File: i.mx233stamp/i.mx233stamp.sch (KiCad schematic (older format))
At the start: 0 parts

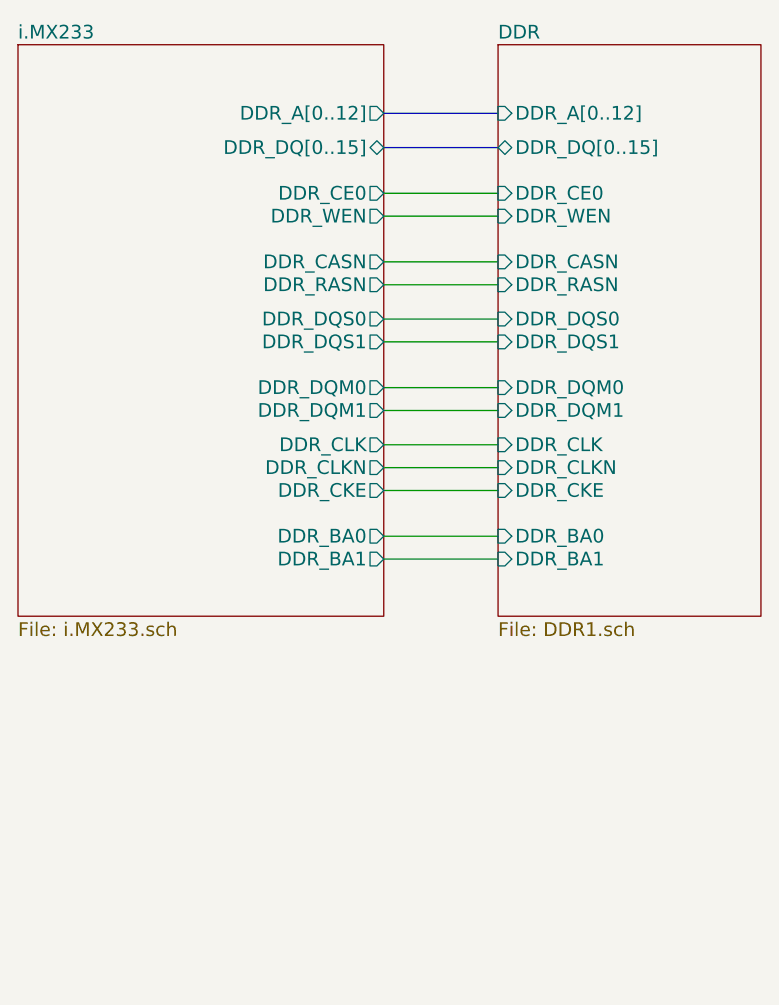
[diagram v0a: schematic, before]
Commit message: Added some connections to the pin header and the filters of the sources
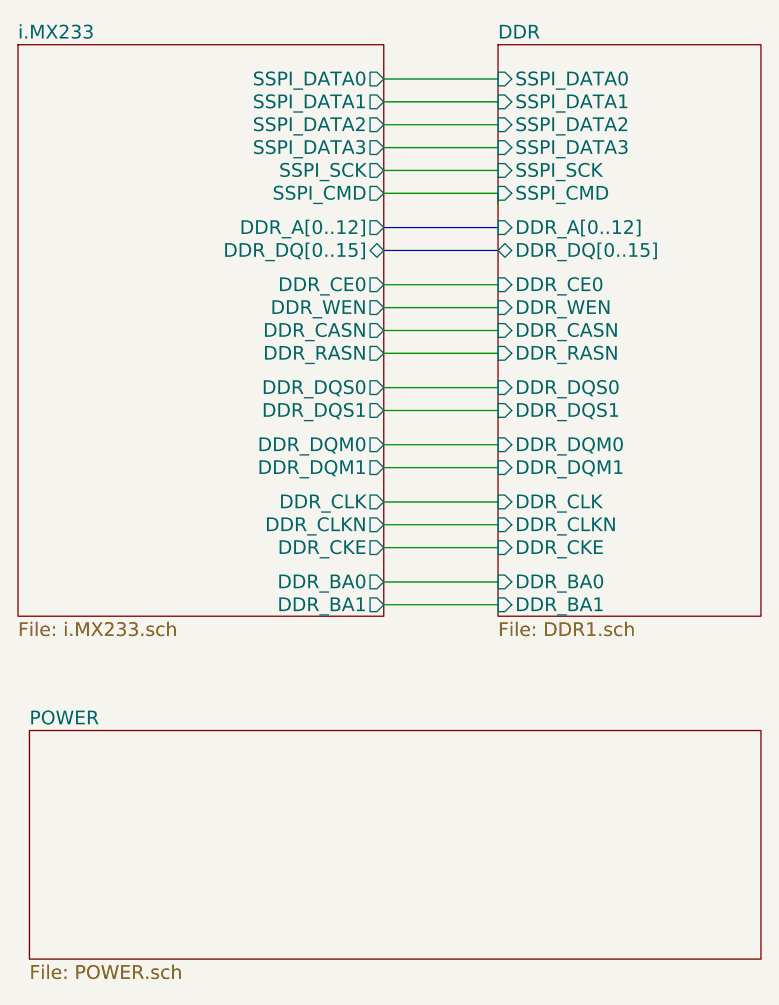
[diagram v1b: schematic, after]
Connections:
- wire segments 13 -> 20
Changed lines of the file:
@@
-EESchema Schematic File Version 2  date Thu 20 Jan 2011 08:06:53 AM COT
+EESchema Schematic File Version 2  date jue 27 ene 2011 16:12:42 COT
+LIBS:transistor-npn
+LIBS:ipc-7351-transistor
+LIBS:switch-misc
 LIBS:power
 LIBS:device
@@
 LIBS:EEPROM
 LIBS:PWR
+LIBS:m25p32
 LIBS:i.mx233stamp-cache
 EELAYER 24  0
 EELAYER END
 $Descr A4 11700 8267
-Sheet 1 3
+Sheet 1 4
 Title ""
-Date "20 jan 2011"
+Date "27 jan 2011"
 Rev ""
 Comp ""
@@
 Comment4 ""
 $EndDescr
+$Sheet
+S 3200 4600 3200 1000
+U 4D41BD76
+F0 "POWER" 60
+F1 "POWER.sch" 60
+$EndSheet
 Wire Wire Line
-	4750 3200 5250 3200
+	4750 2150 5250 2150
 Wire Wire Line
-	5250 2900 4750 2900
+	4750 1850 5250 1850
+Wire Bus Line
+	4750 2500 5250 2500
+Wire Wire Line
+	4750 2050 5250 2050
+Wire Wire Line
+	5250 3350 4750 3350
+Wire Wire Line
+	4750 3100 5250 3100
+Wire Wire Line
+	4750 3950 5250 3950
+Wire Wire Line
+	4750 3700 5250 3700
 Wire Wire Line
 	4750 2650 5250 2650
 Wire Wire Line
-	4750 3850 5250 3850
+	4750 2750 5250 2750
 Wire Wire Line
-	4750 3550 5250 3550
+	4750 2850 5250 2850
 Wire Wire Line
-	4750 3350 5250 3350
+	4750 3600 5250 3600
 Wire Wire Line
-	4750 2550 5250 2550
+	4750 3800 5250 3800
 Wire Wire Line
-	4750 2250 5250 2250
-Wire Bus Line
-	4750 1900 5250 1900
-Wire Bus Line
-	4750 2050 5250 2050
+	4750 4050 5250 4050
 Wire Wire Line
-	4750 2350 5250 2350
+	4750 2950 5250 2950
+Wire Wire Line
+	5250 3200 4750 3200
 Wire Wire Line
 	4750 3450 5250 3450
+Wire Bus Line
+	5250 2400 4750 2400
 Wire Wire Line
-	4750 3750 5250 3750
+	5250 1750 4750 1750
 Wire Wire Line
-	4750 2800 5250 2800
+	5250 1950 4750 1950
 Wire Wire Line
-	5250 3100 4750 3100
+	5250 2300 5250 2250
+Wire Wire Line
+	5250 2250 4750 2250
 $Sheet
 S 5250 1600 1150 2500
@@
 F0 "DDR" 60
 F1 "DDR1.sch" 60
-F2 "DDR_A[0..12]" I L 5250 1900 60
-F3 "DDR_DQ[0..15]" B L 5250 2050 60
-F4 "DDR_BA0" I L 5250 3750 60
-F5 "DDR_BA1" I L 5250 3850 60
-F6 "DDR_CE0" I L 5250 2250 60
-F7 "DDR_CASN" I L 5250 2550 60
-F8 "DDR_CKE" I L 5250 3550 60
-F9 "DDR_CLKN" I L 5250 3450 60
-F10 "DDR_CLK" I L 5250 3350 60
-F11 "DDR_DQM0" I L 5250 3100 60
-F12 "DDR_DQM1" I L 5250 3200 60
-F13 "DDR_DQS0" I L 5250 2800 60
-F14 "DDR_DQS1" I L 5250 2900 60
-F15 "DDR_RASN" I L 5250 2650 60
-F16 "DDR_WEN" I L 5250 2350 60
+F2 "DDR_A[0..12]" I L 5250 2400 60
+F3 "DDR_DQ[0..15]" B L 5250 2500 60
+F4 "DDR_BA0" I L 5250 3950 60
+F5 "DDR_BA1" I L 5250 4050 60
+F6 "DDR_CE0" I L 5250 2650 60
+F7 "DDR_CASN" I L 5250 2850 60
+F8 "DDR_CKE" I L 5250 3800 60
+F9 "DDR_CLKN" I L 5250 3700 60
+F10 "DDR_CLK" I L 5250 3600 60
+F11 "DDR_DQM0" I L 5250 3350 60
+F12 "DDR_DQM1" I L 5250 3450 60
+F13 "DDR_DQS0" I L 5250 3100 60
+F14 "DDR_DQS1" I L 5250 3200 60
+F15 "DDR_RASN" I L 5250 2950 60
+F16 "DDR_WEN" I L 5250 2750 60
+F17 "SSPI_DATA3" I L 5250 2050 60
+F18 "SSPI_DATA2" I L 5250 1950 60
+F19 "SSPI_SCK" I L 5250 2150 60
+F20 "SSPI_CMD" I L 5250 2250 60
+F21 "SSPI_DATA1" I L 5250 1850 60
+F22 "SSPI_DATA0" I L 5250 1750 60
 $EndSheet
 $Sheet
@@
 F0 "i.MX233" 60
 F1 "i.MX233.sch" 60
-F2 "DDR_A[0..12]" O R 4750 1900 60
-F3 "DDR_DQ[0..15]" B R 4750 2050 60
-F4 "DDR_WEN" O R 4750 2350 60
-F5 "DDR_RASN" O R 4750 2650 60
-F6 "DDR_DQS1" O R 4750 2900 60
-F7 "DDR_DQS0" O R 4750 2800 60
-F8 "DDR_DQM1" O R 4750 3200 60
-F9 "DDR_DQM0" O R 4750 3100 60
-F10 "DDR_CLK" O R 4750 3350 60
-F11 "DDR_CLKN" O R 4750 3450 60
-F12 "DDR_CKE" O R 4750 3550 60
-F13 "DDR_CASN" O R 4750 2550 60
-F14 "DDR_CE0" O R 4750 2250 60
-F15 "DDR_BA1" O R 4750 3850 60
-F16 "DDR_BA0" O R 4750 3750 60
+F2 "DDR_A[0..12]" O R 4750 2400 60
+F3 "DDR_DQ[0..15]" B R 4750 2500 60
+F4 "DDR_WEN" O R 4750 2750 60
+F5 "DDR_RASN" O R 4750 2950 60
+F6 "DDR_DQS1" O R 4750 3200 60
+F7 "DDR_DQS0" O R 4750 3100 60
+F8 "DDR_DQM1" O R 4750 3450 60
+F9 "DDR_DQM0" O R 4750 3350 60
+F10 "DDR_CLK" O R 4750 3600 60
+F11 "DDR_CLKN" O R 4750 3700 60
+F12 "DDR_CKE" O R 4750 3800 60
+F13 "DDR_CASN" O R 4750 2850 60
+F14 "DDR_CE0" O R 4750 2650 60
+F15 "DDR_BA1" O R 4750 4050 60
+F16 "DDR_BA0" O R 4750 3950 60
+F17 "SSPI_DATA3" O R 4750 2050 60
+F18 "SSPI_SCK" O R 4750 2150 60
+F19 "SSPI_CMD" O R 4750 2250 60
+F20 "SSPI_DATA0" O R 4750 1750 60
+F21 "SSPI_DATA1" O R 4750 1850 60
+F22 "SSPI_DATA2" O R 4750 1950 60
 $EndSheet
 $EndSCHEMATC

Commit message: Corrected some signals of uSD card
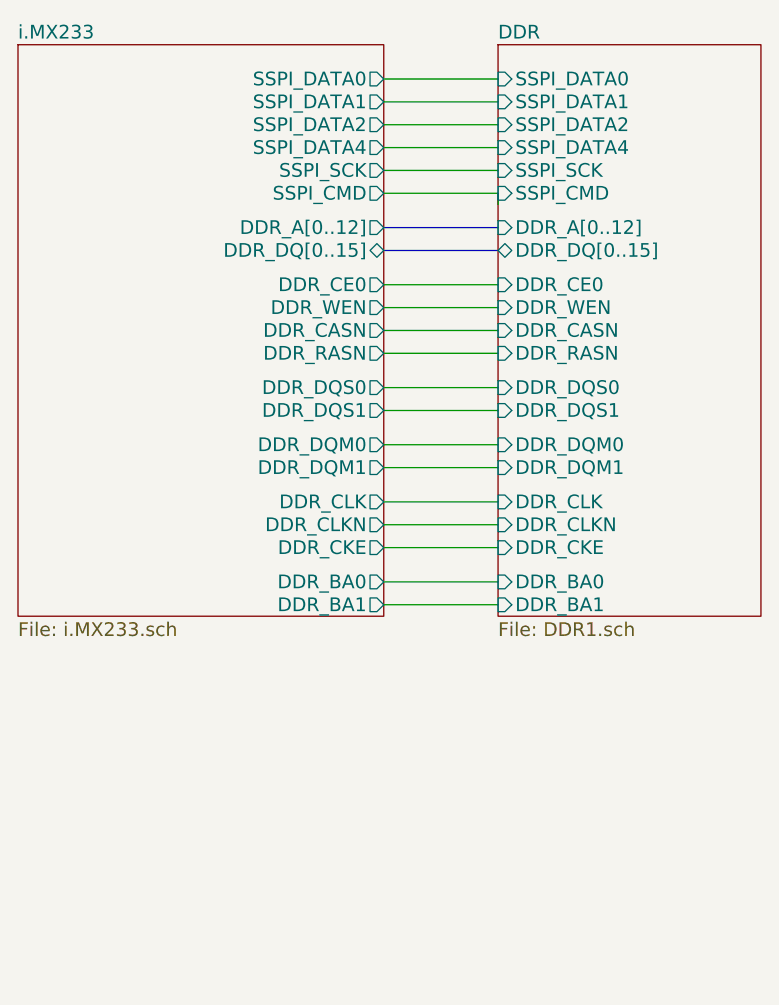
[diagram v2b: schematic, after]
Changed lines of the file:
@@
-EESchema Schematic File Version 2  date jue 27 ene 2011 16:12:42 COT
+EESchema Schematic File Version 2  date lun 31 ene 2011 15:30:54 COT
 LIBS:transistor-npn
 LIBS:ipc-7351-transistor
@@
 EELAYER END
 $Descr A4 11700 8267
-Sheet 1 4
+Sheet 1 3
 Title ""
-Date "27 jan 2011"
+Date "31 jan 2011"
 Rev ""
 Comp ""
@@
 Comment4 ""
 $EndDescr
-$Sheet
-S 3200 4600 3200 1000
-U 4D41BD76
-F0 "POWER" 60
-F1 "POWER.sch" 60
-$EndSheet
 Wire Wire Line
 	4750 2150 5250 2150
@@
 F15 "DDR_RASN" I L 5250 2950 60
 F16 "DDR_WEN" I L 5250 2750 60
-F17 "SSPI_DATA3" I L 5250 2050 60
+F17 "SSPI_DATA4" I L 5250 2050 60
 F18 "SSPI_DATA2" I L 5250 1950 60
 F19 "SSPI_SCK" I L 5250 2150 60
@@
 F15 "DDR_BA1" O R 4750 4050 60
 F16 "DDR_BA0" O R 4750 3950 60
-F17 "SSPI_DATA3" O R 4750 2050 60
+F17 "SSPI_DATA4" O R 4750 2050 60
 F18 "SSPI_SCK" O R 4750 2150 60
 F19 "SSPI_CMD" O R 4750 2250 60
